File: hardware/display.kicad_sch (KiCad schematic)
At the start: 8 parts, among them U6 AP3019AKTR

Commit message: 📂 PCB updates
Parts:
- C27: value 4.7uF/16V -> 4.7uF; footprint (none) -> Capacitor_SMD:C_0603_1608Metric
- C28: footprint (none) -> Capacitor_SMD:C_0805_2012Metric
- L4: footprint (none) -> Inductor_SMD:L_1210_3225Metric
- R11: footprint (none) -> Resistor_SMD:R_0805_2012Metric
- R12: footprint (none) -> Resistor_SMD:R_0603_1608Metric
- TP4: footprint TestPoint:TestPoint_Loop_D2.50mm_Drill1.0mm -> TestPoint:TestPoint_Pad_D1.0mm
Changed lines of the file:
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@@
 			)
 		)
-		(property "Footprint" ""
+		(property "Footprint" "Capacitor_SMD:C_0805_2012Metric"
 			(at 233.3752 82.55 0)
 			(effects
@@
 			)
 		)
-		(property "Value" "4.7uF/16V"
+		(property "Value" "4.7uF"
 			(at 193.04 59.69 90)
 			(effects
@@
 			)
 		)
-		(property "Footprint" ""
+		(property "Footprint" "Capacitor_SMD:C_0603_1608Metric"
 			(at 203.2 59.9948 0)
 			(effects
@@
 			)
 		)
-		(property "Footprint" "TestPoint:TestPoint_Loop_D2.50mm_Drill1.0mm"
+		(property "Footprint" "TestPoint:TestPoint_Pad_D1.0mm"
 			(at 234.95 72.39 0)
 			(effects
@@
 			)
 		)
-		(property "Footprint" ""
+		(property "Footprint" "Resistor_SMD:R_0805_2012Metric"
 			(at 219.202 80.01 90)
 			(effects
@@
 			)
 		)
-		(property "Footprint" ""
+		(property "Footprint" "Inductor_SMD:L_1210_3225Metric"
 			(at 199.39 66.04 0)
 			(effects
@@
 			)
 		)
-		(property "Footprint" ""
+		(property "Footprint" "Resistor_SMD:R_0603_1608Metric"
 			(at 192.532 81.28 90)
 			(effects

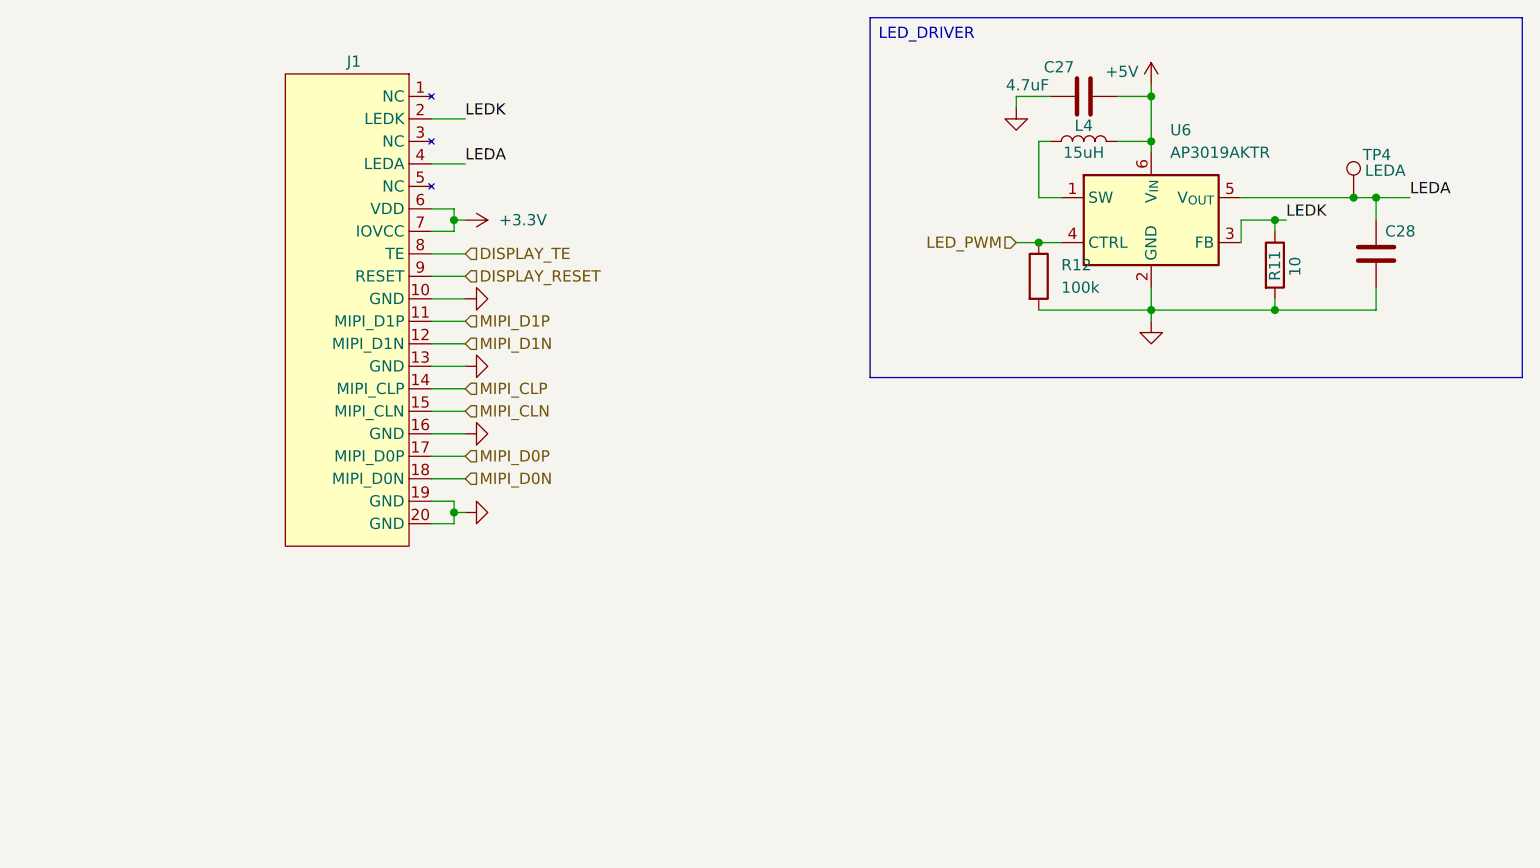
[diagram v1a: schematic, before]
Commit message: 🐛 Fix errors from rev1.0
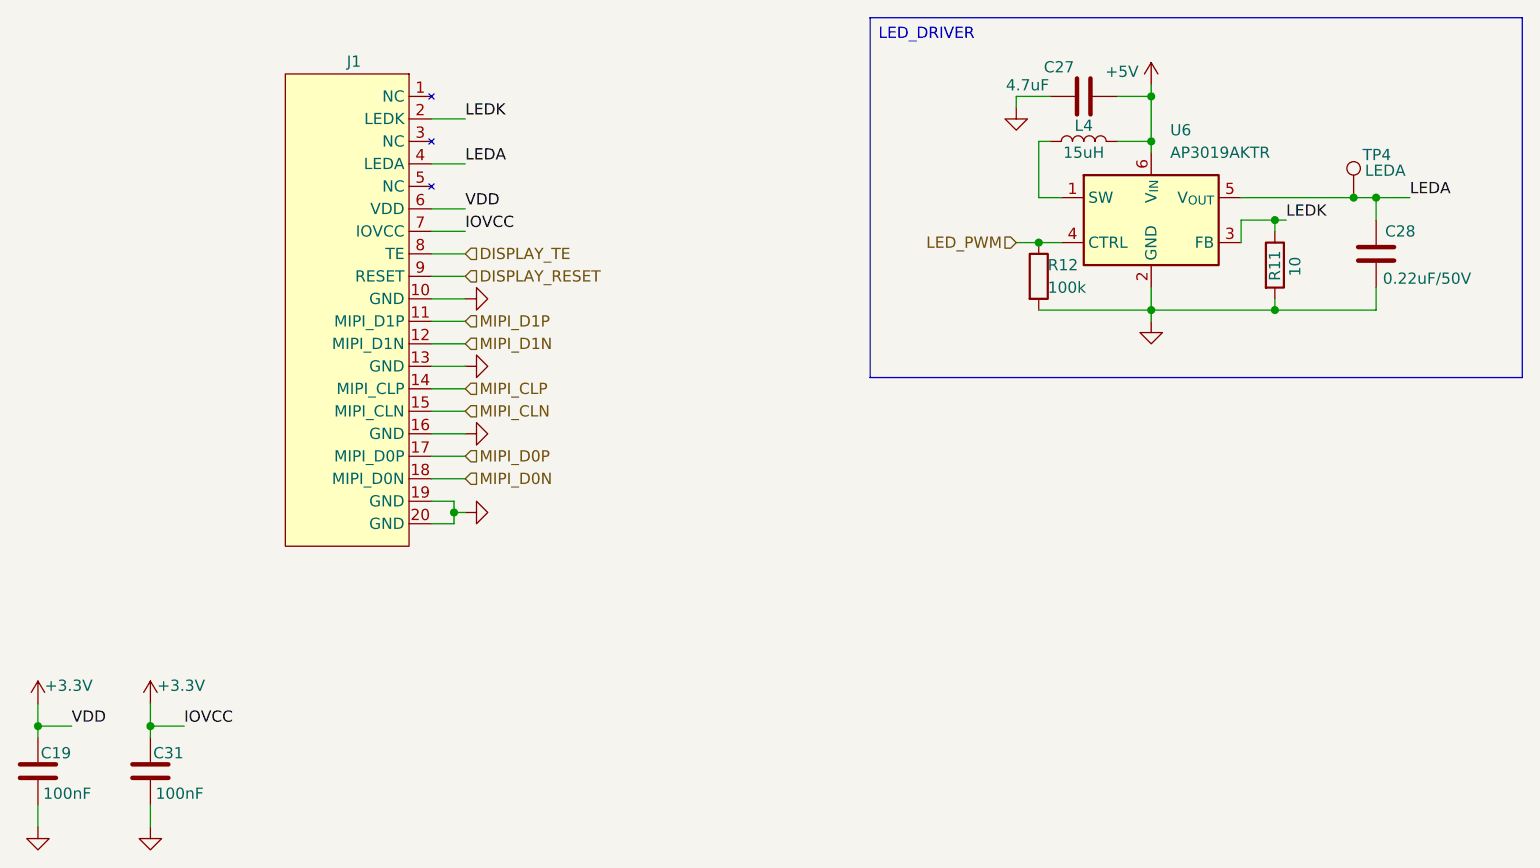
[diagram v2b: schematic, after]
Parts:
- added C19, C31: 100nF, Capacitor_SMD:C_0402_1005Metric, symbol Device:C
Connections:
- net +3.3V: now also C19.1, C31.1
- net GND: now also C19.2, C31.2

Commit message: ✨ Final PCB updates
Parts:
- renumbered C19 to C501, C31 to C502, C27 to C503, C28 to C504, L4 to L501, R12 to R501, R11 to R502, TP4 to TP501, U6 to U501
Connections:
- net +3.3V: no longer C502.1, J1.7 (IOVCC)
- new net +1V8: C502.1, J1.7 (IOVCC)
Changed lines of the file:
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@@
 		(on_board yes)
 		(dnp no)
-		(property "Reference" "C28"
+		(property "Reference" "C504"
 			(at 233.426 76.2 0)
 			(effects
@@
 			(project "peak"
 				(path "/54a54a18-4a65-4728-b17a-32b4a97370c1/4888a3b7-e0e1-4fe3-83ae-3b123e53f2dc"
-					(reference "C28")
+					(reference "C504")
 					(unit 1)
 				)
@@
 		(on_board yes)
 		(dnp no)
-		(property "Reference" "C27"
+		(property "Reference" "C503"
 			(at 196.596 57.658 90)
 			(effects
@@
 			(project "peak"
 				(path "/54a54a18-4a65-4728-b17a-32b4a97370c1/4888a3b7-e0e1-4fe3-83ae-3b123e53f2dc"
-					(reference "C27")
+					(reference "C503")
 					(unit 1)
 				)
@@
 		(on_board yes)
 		(dnp no)
-		(property "Reference" "TP4"
+		(property "Reference" "TP501"
 			(at 230.886 67.564 0)
 			(effects
@@
 			(project "peak"
 				(path "/54a54a18-4a65-4728-b17a-32b4a97370c1/4888a3b7-e0e1-4fe3-83ae-3b123e53f2dc"
-					(reference "TP4")
+					(reference "TP501")
 					(unit 1)
 				)
@@
 	)
 	(symbol
+		(lib_id "power:+1V8")
+		(at 93.98 129.54 0)
+		(unit 1)
+		(exclude_from_sim no)
+		(in_bom yes)
+		(on_board yes)
+		(dnp no)
+		(property "Reference" "#PWR0501"
+			(at 93.98 133.35 0)
+			(effects
+				(font
+					(size 1.27 1.27)
+				)
+				(hide yes)
+			)
+		)
+		(property "Value" "+1V8"
+			(at 96.774 127 0)
+			(effects
+				(font
+					(size 1.27 1.27)
+				)
+			)
+		)
+		(property "Footprint" ""
+			(at 93.98 129.54 0)
+			(effects
+				(font
+					(size 1.27 1.27)
+				)
+				(hide yes)
+			)
+		)
+		(property "Datasheet" ""
+			(at 93.98 129.54 0)
+			(effects
+				(font
+					(size 1.27 1.27)
+				)
+				(hide yes)
+			)
+		)
+		(property "Description" "Power symbol creates a global label with name \"+1V8\""
+			(at 93.98 129.54 0)
+			(effects
+				(font
+					(size 1.27 1.27)
+				)
+				(hide yes)
+			)
+		)
+		(pin "1"
+		)
+		(instances
+			(project "peak"
+				(path "/54a54a18-4a65-4728-b17a-32b4a97370c1/4888a3b7-e0e1-4fe3-83ae-3b123e53f2dc"
+					(reference "#PWR0501")
+					(unit 1)
+				)
+			)
+		)
+	)
+	(symbol
 		(lib_id "power:GND")
 		(at 207.01 86.36 0)
@@
 		(dnp no)
 		(fields_autoplaced yes)
-		(property "Reference" "#PWR019"
+		(property "Reference" "#PWR0181"
 			(at 207.01 92.71 0)
 			(effects
@@
 			(project "peak"
 				(path "/54a54a18-4a65-4728-b17a-32b4a97370c1/4888a3b7-e0e1-4fe3-83ae-3b123e53f2dc"
-					(reference "#PWR019")
+					(reference "#PWR0181")
 					(unit 1)
 				)
@@
 		(on_board yes)
 		(dnp no)
-		(property "Reference" "#PWR013"
+		(property "Reference" "#PWR0183"
 			(at 207.01 63.5 0)
 			(effects
@@
 			(project "peak"
 				(path "/54a54a18-4a65-4728-b17a-32b4a97370c1/4888a3b7-e0e1-4fe3-83ae-3b123e53f2dc"
-					(reference "#PWR013")
-					(unit 1)
-				)
-			)
-		)
-	)
-	(symbol
-		(lib_id "power:+3.3V")
-		(at 93.98 129.54 0)
-		(unit 1)
-		(exclude_from_sim no)
-		(in_bom yes)
-		(on_board yes)
-		(dnp no)
-		(property "Reference" "#PWR054"
-			(at 93.98 133.35 0)
-			(effects
-				(font
-					(size 1.27 1.27)
-				)
-				(hide yes)
-			)
-		)
-		(property "Value" "+3.3V"
-			(at 94.742 127.508 0)
-			(effects
-				(font
-					(size 1.27 1.27)
-				)
-				(justify left)
-			)
-		)
-		(property "Footprint" ""
-			(at 93.98 129.54 0)
-			(effects
-				(font
-					(size 1.27 1.27)
-				)
-				(hide yes)
-			)
-		)
-		(property "Datasheet" ""
-			(at 93.98 129.54 0)
-			(effects
-				(font
-					(size 1.27 1.27)
-				)
-				(hide yes)
-			)
-		)
-		(property "Description" "Power symbol creates a global label with name \"+3.3V\""
-			(at 93.98 129.54 0)
-			(effects
-				(font
-					(size 1.27 1.27)
-				)
-				(hide yes)
-			)
-		)
-		(pin "1"
-		)
-		(instances
-			(project "peak"
-				(path "/54a54a18-4a65-4728-b17a-32b4a97370c1/4888a3b7-e0e1-4fe3-83ae-3b123e53f2dc"
-					(reference "#PWR054")
+					(reference "#PWR0183")
 					(unit 1)
 				)
@@
 		(dnp no)
 		(fields_autoplaced yes)
-		(property "Reference" "#PWR059"
+		(property "Reference" "#PWR0173"
 			(at 135.89 107.95 0)
 			(effects
@@
 			(project ""
 				(path "/54a54a18-4a65-4728-b17a-32b4a97370c1/4888a3b7-e0e1-4fe3-83ae-3b123e53f2dc"
-					(reference "#PWR059")
+					(reference "#PWR0173")
 					(unit 1)
 				)
@@
 		(dnp no)
 		(fields_autoplaced yes)
-		(property "Reference" "U6"
+		(property "Reference" "U501"
 			(at 209.1533 64.77 0)
 			(effects
@@
 			(project "peak"
 				(path "/54a54a18-4a65-4728-b17a-32b4a97370c1/4888a3b7-e0e1-4fe3-83ae-3b123e53f2dc"
-					(reference "U6")
+					(reference "U501")
 					(unit 1)
 				)
@@
 		(dnp no)
 		(fields_autoplaced yes)
-		(property "Reference" "#PWR0114"
+		(property "Reference" "#PWR0179"
 			(at 93.98 149.86 0)
 			(effects
@@
 			(project "peak"
 				(path "/54a54a18-4a65-4728-b17a-32b4a97370c1/4888a3b7-e0e1-4fe3-83ae-3b123e53f2dc"
-					(reference "#PWR0114")
+					(reference "#PWR0179")
 					(unit 1)
 				)
@@
 		(dnp no)
 		(fields_autoplaced yes)
-		(property "Reference" "#PWR060"
+		(property "Reference" "#PWR0175"
 			(at 135.89 99.06 0)
 			(effects
@@
 			(project "peak"
 				(path "/54a54a18-4a65-4728-b17a-32b4a97370c1/4888a3b7-e0e1-4fe3-83ae-3b123e53f2dc"
-					(reference "#PWR060")
+					(reference "#PWR0175")
 					(unit 1)
 				)
@@
 		(dnp no)
 		(fields_autoplaced yes)
-		(property "Reference" "#PWR061"
+		(property "Reference" "#PWR0174"
 			(at 135.89 91.44 0)
 			(effects
@@
 			(project "peak"
 				(path "/54a54a18-4a65-4728-b17a-32b4a97370c1/4888a3b7-e0e1-4fe3-83ae-3b123e53f2dc"
-					(reference "#PWR061")
+					(reference "#PWR0174")
 					(unit 1)
 				)
@@
 		(on_board yes)
 		(dnp no)
-		(property "Reference" "C19"
-			(at 83.312 135.128 0)
+		(property "Reference" "C501"
+			(at 83.82 135.128 0)
 			(effects
 				(font
@@
 			(project "peak"
 				(path "/54a54a18-4a65-4728-b17a-32b4a97370c1/4888a3b7-e0e1-4fe3-83ae-3b123e53f2dc"
-					(reference "C19")
+					(reference "C501")
 					(unit 1)
 				)
@@
 		(on_board yes)
 		(dnp no)
-		(property "Reference" "C31"
-			(at 96.012 135.128 0)
+		(property "Reference" "C502"
+			(at 96.52 135.128 0)
 			(effects
 				(font
@@
 			(project "peak"
 				(path "/54a54a18-4a65-4728-b17a-32b4a97370c1/4888a3b7-e0e1-4fe3-83ae-3b123e53f2dc"
-					(reference "C31")
+					(reference "C502")
 					(unit 1)
 				)
@@
 		(dnp no)
 		(fields_autoplaced yes)
-		(property "Reference" "#PWR020"
+		(property "Reference" "#PWR0182"
 			(at 191.77 68.58 0)
 			(effects
@@
 			(project "peak"
 				(path "/54a54a18-4a65-4728-b17a-32b4a97370c1/4888a3b7-e0e1-4fe3-83ae-3b123e53f2dc"
-					(reference "#PWR020")
+					(reference "#PWR0182")
 					(unit 1)
 				)
@@
 		(dnp no)
 		(fields_autoplaced yes)
-		(property "Reference" "#PWR062"
+		(property "Reference" "#PWR0176"
 			(at 135.89 83.82 0)
 			(effects
@@
 			(project "peak"
 				(path "/54a54a18-4a65-4728-b17a-32b4a97370c1/4888a3b7-e0e1-4fe3-83ae-3b123e53f2dc"
-					(reference "#PWR062")
+					(reference "#PWR0176")
 					(unit 1)
 				)
@@
 		(on_board yes)
 		(dnp no)
-		(property "Reference" "#PWR063"
+		(property "Reference" "#PWR0178"
 			(at 81.28 133.35 0)
 			(effects
@@
 			(project "peak"
 				(path "/54a54a18-4a65-4728-b17a-32b4a97370c1/4888a3b7-e0e1-4fe3-83ae-3b123e53f2dc"
-					(reference "#PWR063")
+					(reference "#PWR0178")
 					(unit 1)
 				)
@@
 		(dnp no)
 		(fields_autoplaced yes)
-		(property "Reference" "#PWR053"
+		(property "Reference" "#PWR0180"
 			(at 81.28 149.86 0)
 			(effects
@@
 			(project "peak"
 				(path "/54a54a18-4a65-4728-b17a-32b4a97370c1/4888a3b7-e0e1-4fe3-83ae-3b123e53f2dc"
-					(reference "#PWR053")
+					(reference "#PWR0180")
 					(unit 1)
 				)
@@
 		(on_board yes)
 		(dnp no)
-		(property "Reference" "R11"
+		(property "Reference" "R502"
 			(at 220.98 81.788 90)
 			(effects
@@
 			(project "peak"
 				(path "/54a54a18-4a65-4728-b17a-32b4a97370c1/4888a3b7-e0e1-4fe3-83ae-3b123e53f2dc"
-					(reference "R11")
+					(reference "R502")
 					(unit 1)
 				)
@@
 		(on_board yes)
 		(dnp no)
-		(property "Reference" "L4"
+		(property "Reference" "L501"
 			(at 199.39 64.262 90)
 			(effects
@@
 			(project "peak"
 				(path "/54a54a18-4a65-4728-b17a-32b4a97370c1/4888a3b7-e0e1-4fe3-83ae-3b123e53f2dc"
-					(reference "L4")
+					(reference "L501")
 					(unit 1)
 				)
@@
 		(on_board yes)
 		(dnp no)
-		(property "Reference" "R12"
+		(property "Reference" "R501"
 			(at 195.326 80.01 0)
 			(effects
@@
 			(project "peak"
 				(path "/54a54a18-4a65-4728-b17a-32b4a97370c1/4888a3b7-e0e1-4fe3-83ae-3b123e53f2dc"
-					(reference "R12")
-					(unit 1)
-				)
+					(reference "R501")
+					(unit 1)
+				)
